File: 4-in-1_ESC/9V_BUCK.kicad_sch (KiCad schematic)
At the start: 4 parts, among them U9 STM32G071GBU6

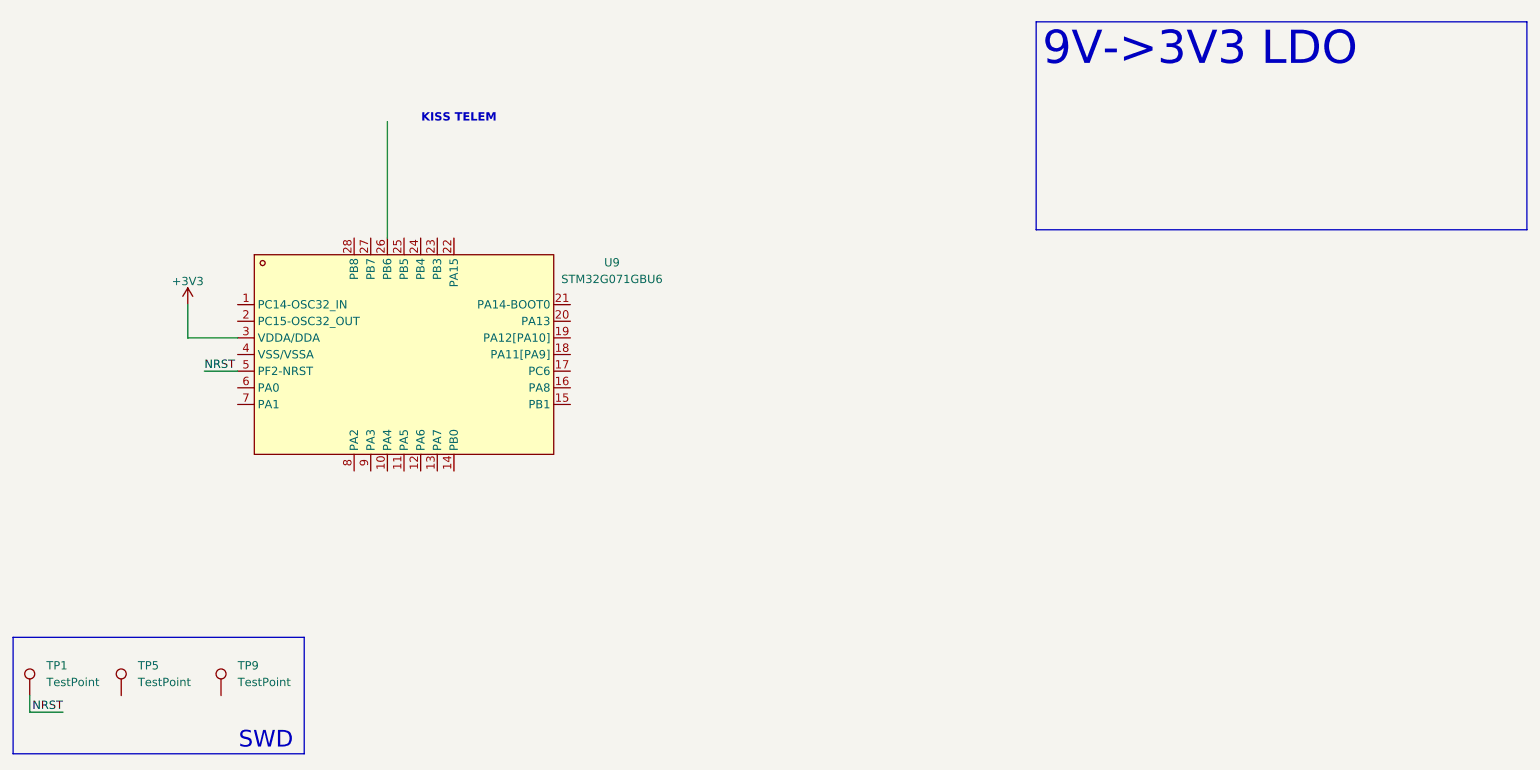
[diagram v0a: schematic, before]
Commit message: Schematic Updates
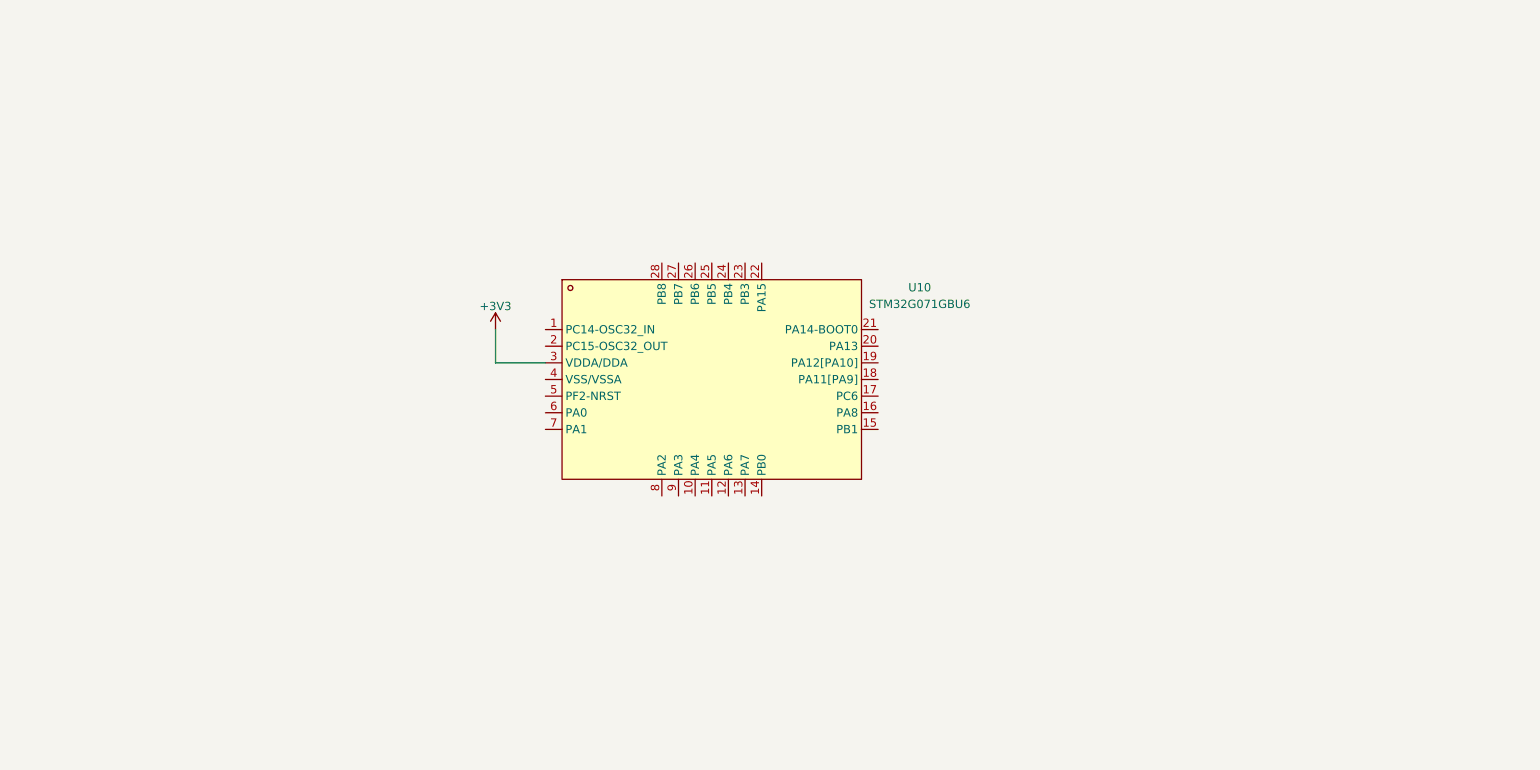
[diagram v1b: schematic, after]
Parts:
- removed TP1, TP5, TP9: TestPoint, symbol Connector:TestPoint
- renumbered U9 to U10
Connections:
- net NRST: no longer names the net of U10.5 (PF2-NRST)
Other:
- note removed: "KISS TELEM"
- note removed: "SWD"
- moved on the sheet: U10
